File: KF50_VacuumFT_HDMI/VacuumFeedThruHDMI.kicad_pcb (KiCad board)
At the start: 4 copper layers, 142 x 154 mm, 13 parts, among them J1 DB25_Male, J1_(11:12) HDMI_A_1.4, J1_(1:5) HDMI_A_1.4, J1_(6:10) HDMI_A_1.4, J2 Conn_01x08, J2 DB25_Male, J2_(11:12) HDMI_A_1.4, J2_(1:5) HDMI_A_1.4, J2_(6:10) HDMI_A_1.4, J3 DB25_Male, J3_(11:12) HDMI_A_1.4, J3_(1:5) HDMI_A_1.4, J3_(6:10) HDMI_A_1.4

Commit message: ReUpdate
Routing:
- net Net-(J1-Pad6): track 0.00 -> 50.6 mm
- net Net-(J1-Pad4): track 0.00 -> 49.6 mm
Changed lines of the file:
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@@
     (thickness 1.6)
     (drawings 34)
-    (tracks 434)
+    (tracks 442)
     (zones 0)
     (modules 13)
@@
   (page A4)
   (layers
-    (0 F.Cu signal hide)
+    (0 F.Cu signal)
     (1 In1.Cu signal)
     (2 In2.Cu signal)
@@
       (outputformat 1)
       (mirror false)
-      (drillshape 1)
+      (drillshape 0)
       (scaleselection 1)
-      (outputdirectory ""))
+      (outputdirectory "Gerber/"))
   )
   (net 0 "")
@@
   (segment (start 1.27 -12) (end 1.27 -13.345602) (width 0.09) (layer In1.Cu) (net 13))
   (segment (start -6.800428 -21.469572) (end -6.800428 -55.240428) (width 0.09) (layer In1.Cu) (net 13))
+  (segment (start 0.9 -61) (end 2.39 -61) (width 0.09) (layer In2.Cu) (net 14))
+  (segment (start 2.39 -61) (end 2.93 -60.46) (width 0.09) (layer In2.Cu) (net 14))
+  (segment (start 2.93 -15.395) (end 0.635 -13.1) (width 0.09) (layer In2.Cu) (net 14))
+  (segment (start 2.93 -60.46) (end 2.93 -15.395) (width 0.09) (layer In2.Cu) (net 14))
+  (segment (start 2.38501 -58.51499) (end 0.9 -60) (width 0.09) (layer In2.Cu) (net 16))
+  (segment (start 2.38501 -55.883417) (end 2.38501 -58.51499) (width 0.09) (layer In2.Cu) (net 16))
+  (segment (start 0 -53.498407) (end 2.38501 -55.883417) (width 0.09) (layer In2.Cu) (net 16))
+  (segment (start 0 -12) (end 0 -53.498407) (width 0.09) (layer In2.Cu) (net 16))
   (segment (start -0.635 -13.1) (end -6.99497 -19.45997) (width 0.09) (layer In1.Cu) (net 17))
   (segment (start -0.718198 -57.89) (end -4.405428 -57.89) (width 0.09) (layer In1.Cu) (net 17))

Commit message: Update Gerber
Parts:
- J1_(11:12), J1_(1:5), J1_(6:10), J2_(11:12), J2_(1:5), J2_(6:10), J3_(11:12), J3_(1:5), J3_(6:10): value HDMI_A_1.4 -> HDMI-TH_19P-P0.50-M_HDMI-19PM
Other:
- board text added: "VacuumFT_HDMI_V1 August 2021 Ryan Morgenstern Ambient Pressure Side"
- board text added: "VacuumFT_HDMI_V1 August 2021 Ryan Morgenstern Vacuum Side"

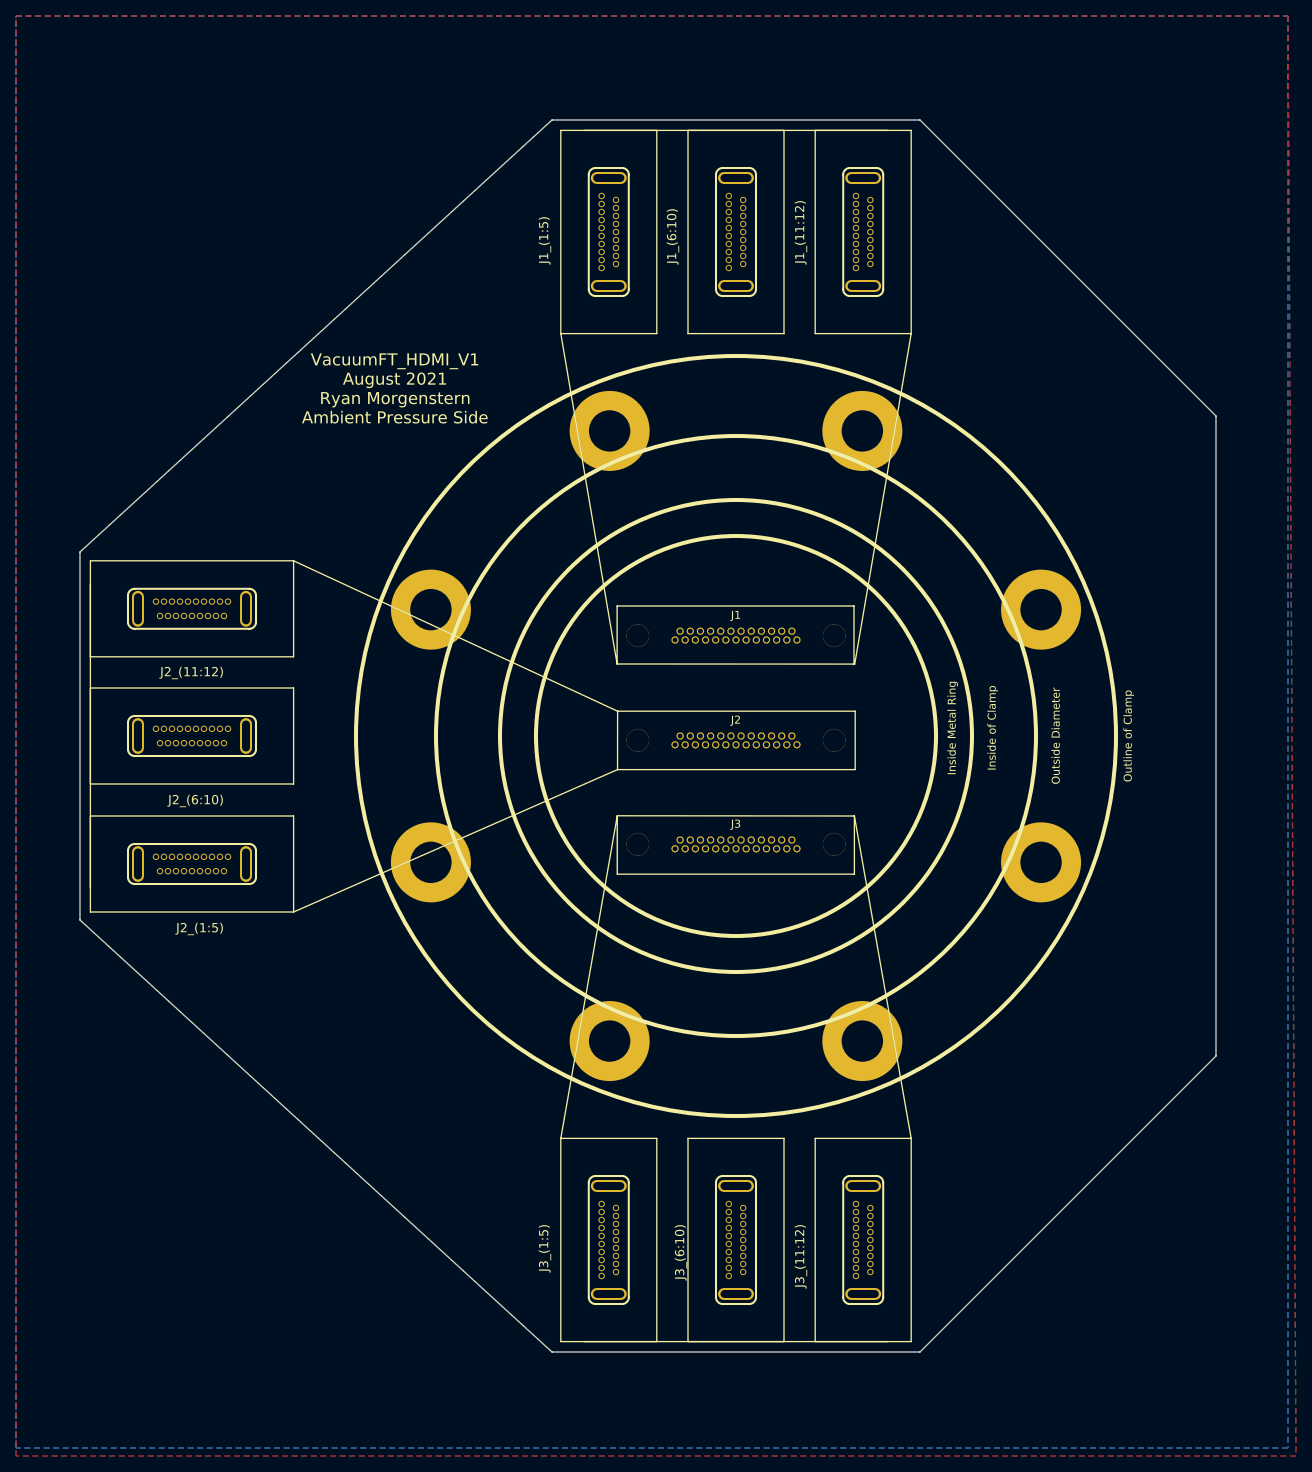
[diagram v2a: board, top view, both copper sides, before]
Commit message: Updated
4 Pair in HDMI
Fixed Gnds
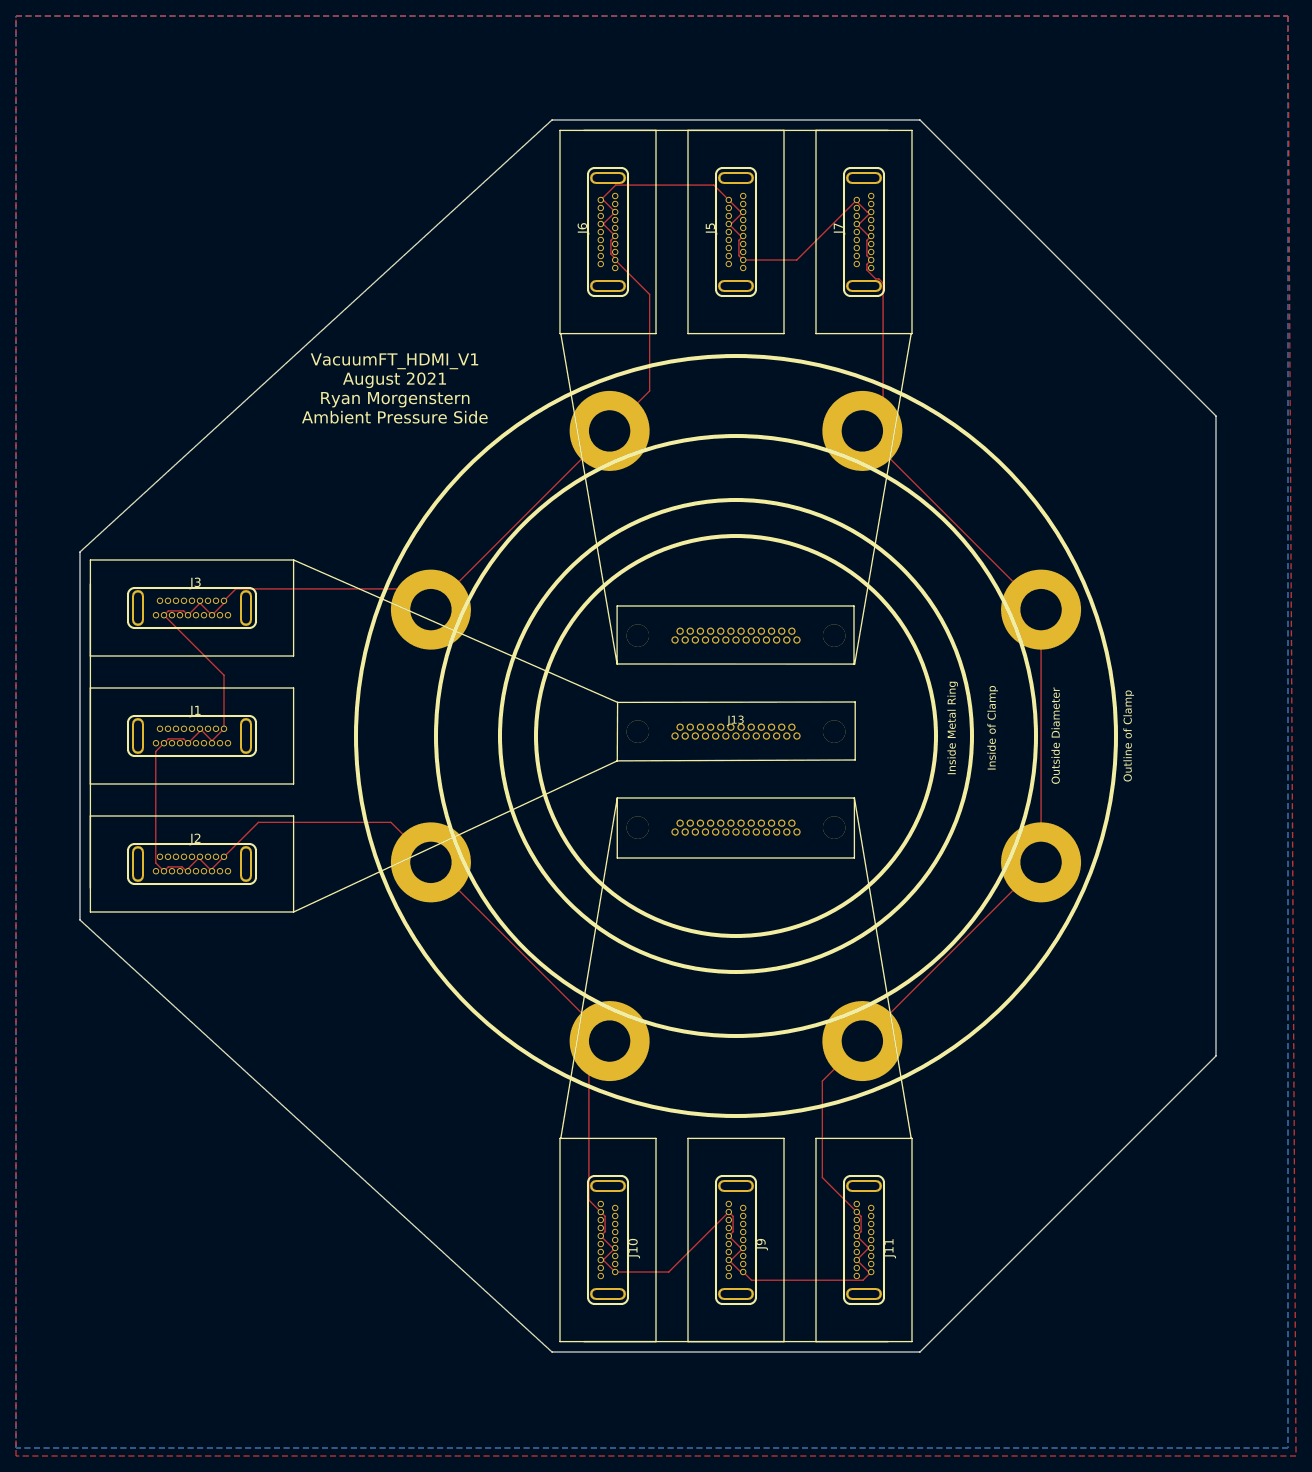
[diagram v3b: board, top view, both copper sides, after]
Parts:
- removed J1_(11:12), J1_(1:5), J1_(6:10), J2_(11:12), J2_(1:5), J2_(6:10), J3_(11:12), J3_(1:5), J3_(6:10): HDMI-TH_19P-P0.50-M_HDMI-19PM, Connector:HDMI-Vertical-Male-JLBPCB
- added J10: HDMI_A_1.4, Connector:HDMI-Vertical-Male-JLBPCB, F.Cu at (-16.0, 63.0)
- added J11: HDMI_A_1.4, Connector:HDMI-Vertical-Male-JLBPCB, F.Cu at (16.0, 63.0)
- added J12: DB25_Male, Connector:Norcomp-380-025-113L001-microd_NoLeads, B.Cu at (0.00, 11.4)
- added J4: DB25_Male, Connector:Norcomp-380-025-113L001-microd_NoLeads, B.Cu at (0.00, -0.55)
- added J5: HDMI_A_1.4, Connector:HDMI-Vertical-Male-JLBPCB, F.Cu at (0.00, -63.0)
- added J6: HDMI_A_1.4, Connector:HDMI-Vertical-Male-JLBPCB, F.Cu at (-16.0, -63.0)
- added J7: HDMI_A_1.4, Connector:HDMI-Vertical-Male-JLBPCB, F.Cu at (16.0, -63.0)
- added J8: DB25_Male, Connector:Norcomp-380-025-113L001-microd_NoLeads, B.Cu at (0.00, -12.6)
- added J9: HDMI_A_1.4, Connector:HDMI-Vertical-Male-JLBPCB, F.Cu at (0.00, 63.0)
- J1, J2, J3: value DB25_Male -> HDMI_A_1.4; footprint Connector:Norcomp-380-025-113L001-microd_NoLeads -> Connector:HDMI-Vertical-Male-JLBPCB; moved to F.Cu
- moved J3 74.1 mm to (-68.0, -16.0)
- moved J2 69.7 mm to (-68.0, 16.0)
- moved J1 69.1 mm to (-68.0, 0.00)
- renumbered J2 to J13
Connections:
- J1 pad 11: Net-(J3-Pad1) (its old number) -> GND
- J1 pad 17: Net-(J2-Pad12) (its old number) -> GND
- J1 pad 2: Net-(J2-Pad4) (its old number) -> GND
- J1 pad 5: Net-(J2-Pad14) (its old number) -> GND
- J1 pad 8: Net-(J1-Pad7) (its old number) -> GND
- J13 pad 1: Net-(J13-Pad1) -> GND
- J13 pad 2: Net-(J13-Pad1) -> GND
- J13 pad 3: Net-(J13-Pad1) -> GND
- J13 pad 4: Net-(J13-Pad1) -> GND
- J13 pad 5: Net-(J13-Pad1) -> GND
- J13 pad 6: Net-(J13-Pad1) -> GND
- J13 pad 7: Net-(J13-Pad1) -> GND
- J13 pad 8: Net-(J13-Pad1) -> GND
- J2 pad 11: Net-(J7-Pad1) -> GND
- J2 pad 17: Net-(J6-Pad12) -> GND
- J2 pad 2: Net-(J6-Pad4) -> GND
- J2 pad 5: Net-(J6-Pad14) -> GND
- J2 pad 8: Net-(J5-Pad7) -> GND
- J3 pad 11: Net-(J11-Pad1) -> GND
- J3 pad 17: Net-(J10-Pad12) -> GND
- J3 pad 2: Net-(J10-Pad4) -> GND
- J3 pad 5: Net-(J10-Pad14) -> GND
- J3 pad 8: Net-(J12-Pad8) -> GND
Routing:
- net GND: track 0.00 -> 510.6 mm
- net Net-(J12-Pad7): track 0.00 -> 97.2 mm
- net Net-(J1-Pad19) (its old number): track 96.2 -> 0.00 mm
- net Net-(J6-Pad14): track 90.8 -> 0.00 mm
- net Net-(J10-Pad14): track 87.2 -> 0.00 mm
- net Net-(J6-Pad7): track 0.00 -> 82.3 mm
- net Net-(J2-Pad19): track 80.4 -> 0.00 mm
- net Net-(J2-Pad15): track 80.1 -> 0.00 mm
- net Net-(J5-Pad19): track 75.6 -> 0.00 mm
- net Net-(J3-Pad15): track 75.6 -> 0.00 mm
- net Net-(J10-Pad9): track 0.00 -> 75.3 mm
- net Net-(J10-Pad7): track 0.00 -> 75.2 mm
- net Net-(J1-Pad18): track 72.3 -> 0.00 mm
- net Net-(J2-Pad16): track 71.8 -> 0.00 mm
- net Net-(J2-Pad14): track 71.6 -> 0.00 mm
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- added copper zone on B.Cu, net GND
- added copper zone on F.Cu, net GND
- added copper zone on In1.Cu, net GND
- added copper zone on In2.Cu, net GND
- removed copper zone on B.Cu, net (none)
- removed copper zone on F.Cu, net (none)
- removed copper zone on In1.Cu, net (none)
- removed copper zone on In2.Cu, net (none)

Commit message: Update
Moved +/- pairs on top of each other
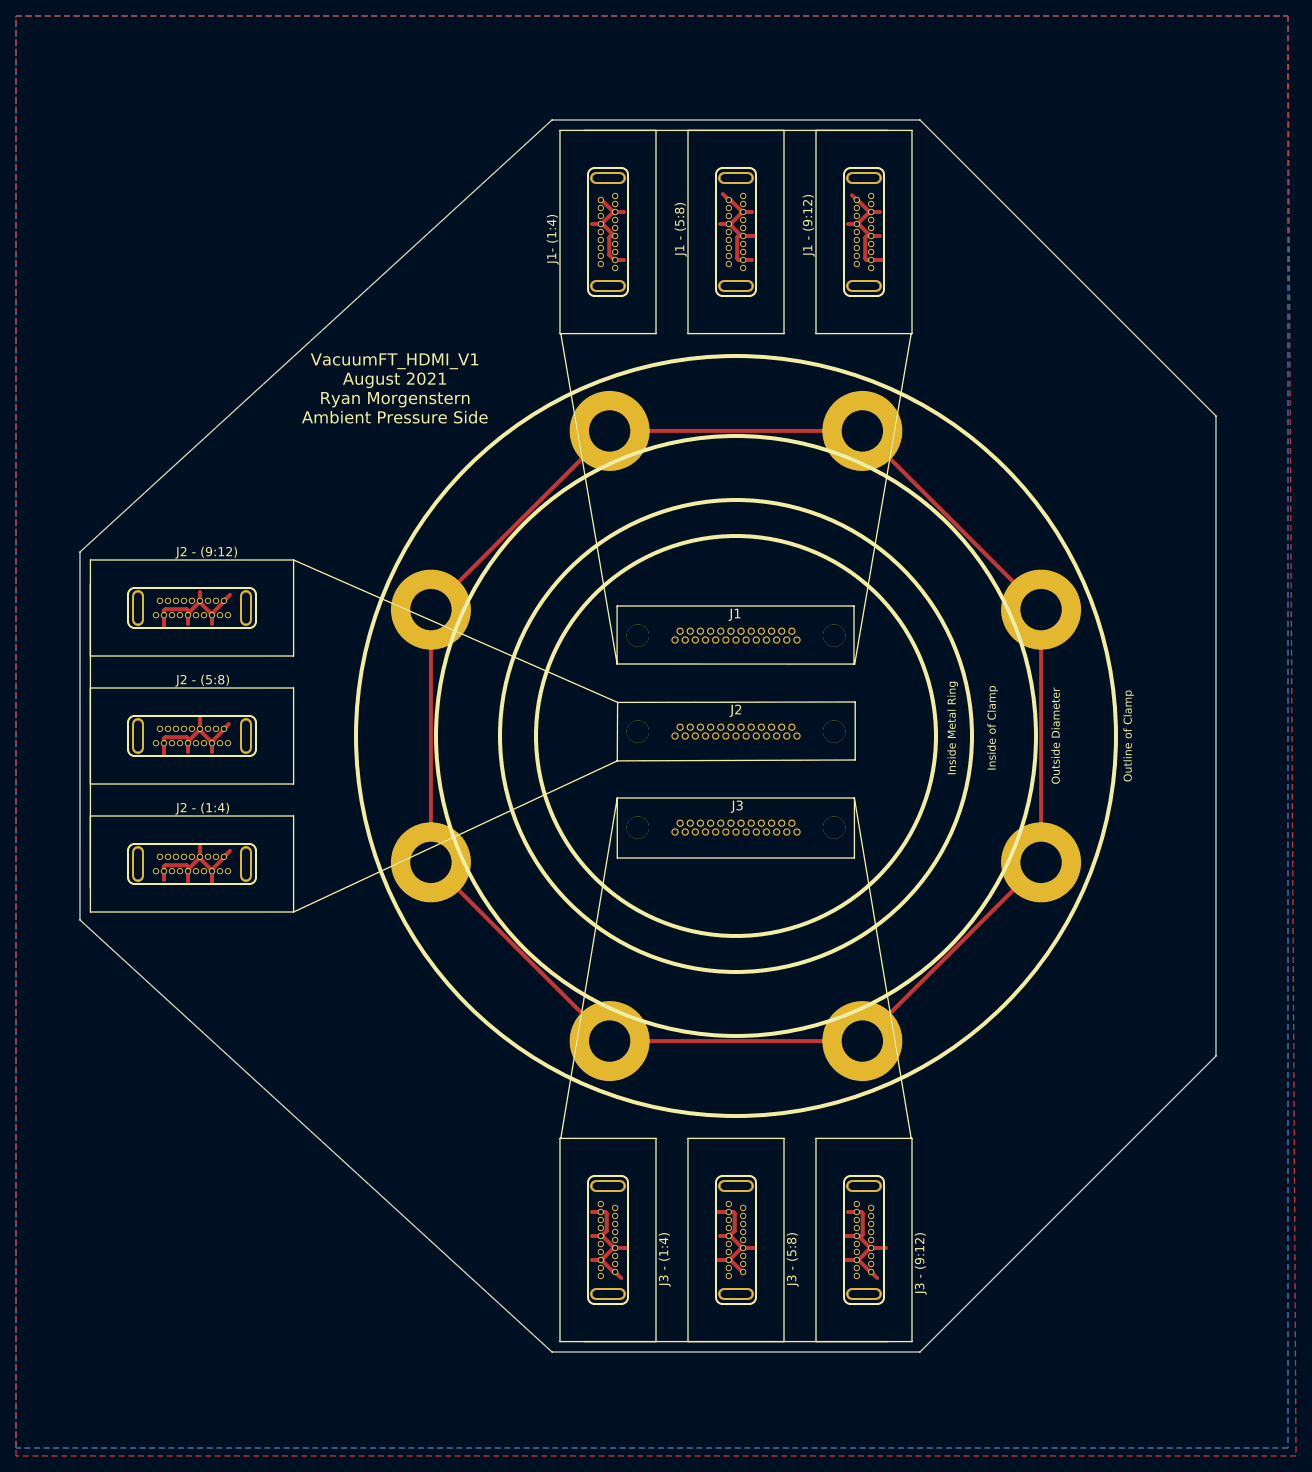
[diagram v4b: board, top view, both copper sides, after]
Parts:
- removed J13: Conn_01x08, Connector:KF50_Print
- removed J6, J7: HDMI_A_1.4, Connector:HDMI-Vertical-Male-JLBPCB
- added ?: , , F.Cu at (1.76, -2.66)
- added ?: , , F.Cu at (2.54, -26.8)
- added ?: , , F.Cu at (-0.36, -15.7)
- added J1 - (9:12): HDMI_A_1.4, Connector:HDMI-Vertical-Male-JLBPCB, F.Cu at (16.0, -63.0)
- added J1- (1:4): HDMI_A_1.4, Connector:HDMI-Vertical-Male-JLBPCB, F.Cu at (-16.0, -63.0)
- added J2: Conn_01x08, Connector:KF50_Print, F.Cu at (0.00, 0.00)
- J1 - (5:8): renamed from J5
- J2 - (1:4): renamed from J2
- J2 - (5:8): renamed from J1
- J2 - (9:12): renamed from J3
- J3 - (1:4): renamed from J10
- J3 - (5:8): renamed from J9
- J3 - (9:12): renamed from J11
- renumbered J8 to J1, J4 to J2, J12 to J3
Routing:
- net GND: track 510.6 -> 404.6 mm
- net Net-(J6-Pad9): track 64.6 -> 84.3 mm
- net Net-(J6-Pad3): track 56.8 -> 71.1 mm
- net Net-(J11-Pad9): track 71.2 -> 57.1 mm
- net Net-(J10-Pad6): track 66.5 -> 58.6 mm
- net Net-(J6-Pad6): track 62.5 -> 67.7 mm
- net Net-(J7-Pad6): track 56.3 -> 61.4 mm
- net Net-(J7-Pad12): track 52.3 -> 56.8 mm
- net Net-(J12-Pad21): track 56.2 -> 52.5 mm
- net Net-(J10-Pad12): track 64.3 -> 67.9 mm
- net Net-(J1-Pad3): track 66.3 -> 69.5 mm
- net Net-(J7-Pad3): track 61.8 -> 64.8 mm
- net Net-(J7-Pad9): track 60.3 -> 63.1 mm
- net Net-(J6-Pad12): track 67.4 -> 65.0 mm
- net Net-(J3-Pad7): track 99.3 -> 101.6 mm
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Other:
- net class GND added: clearance 0.09, trace_width 0.25, via_dia 0.8, via_drill 0.4

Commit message: Updated Gerber
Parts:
- J1_(1:4): renamed from J1- (1:4)
- J1_(5:8): renamed from J1 - (5:8)
- J1_(9:12): renamed from J1 - (9:12)
- J2_(1:4): renamed from J2 - (1:4)
- J2_(5:8): renamed from J2 - (5:8)
- J2_(9:12): renamed from J2 - (9:12)
- J3_(1:4): renamed from J3 - (1:4)
- J3_(5:8): renamed from J3 - (5:8)
- J3_(9:12): renamed from J3 - (9:12)
